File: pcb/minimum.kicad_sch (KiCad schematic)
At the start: 24 parts, among them J1 USB4155-03-C_REVA, U1 RP2040, U2 SCD4x, Y1 C2E-12.000-18-1020-X-R

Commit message: flash added
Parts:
- added U3: W25Q128JVPIM, SMD:W25Q128JVPIM, symbol W25Q128:W25Q128JVPIM
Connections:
- net +3V3: now also U3.8 (VCC)
- net GND: now also U3.4 (GND)
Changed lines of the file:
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@@
+    (pin "1")
+  )
+  (symbol (lib_id "power:+3V3") (at 55.245 147.32 0) (unit 1)
+    (in_bom yes) (on_board yes) (fields_autoplaced)
+    (property "Reference" "#PWR0117" (id 0) (at 55.245 151.13 0)
+      (effects (font (size 1.27 1.27)) hide)
+    )
+    (property "Value" "+3V3" (id 1) (at 55.245 143.7154 0))
+    (property "Footprint" "" (id 2) (at 55.245 147.32 0)
+      (effects (font (size 1.27 1.27)) hide)
+    )
+    (property "Datasheet" "" (id 3) (at 55.245 147.32 0)
+      (effects (font (size 1.27 1.27)) hide)
+    )
     (pin "1")
   )
@@
     )
     (property "Datasheet" "" (id 3) (at 53.975 108.585 0)
+      (effects (font (size 1.27 1.27)) hide)
+    )
+    (pin "1")
+  )
+  (symbol (lib_id "power:GND") (at 55.245 188.595 0) (unit 1)
+    (in_bom yes) (on_board yes) (fields_autoplaced)
+    (property "Reference" "#PWR0118" (id 0) (at 55.245 194.945 0)
+      (effects (font (size 1.27 1.27)) hide)
+    )
+    (property "Value" "GND" (id 1) (at 55.245 193.1576 0))
+    (property "Footprint" "" (id 2) (at 55.245 188.595 0)
+      (effects (font (size 1.27 1.27)) hide)
+    )
+    (property "Datasheet" "" (id 3) (at 55.245 188.595 0)
       (effects (font (size 1.27 1.27)) hide)
     )
@@
     (pin "S1")
     (pin "S2")
+  )
+  (symbol (lib_id "W25Q128:W25Q128JVPIM") (at 55.245 167.64 0) (unit 1)
+    (in_bom yes) (on_board yes)
+    (property "Reference" "U3" (id 0) (at 44.1325 153.33 0)
+      (effects (font (size 1.524 1.524)))
+    )
+    (property "Value" "W25Q128JVPIM" (id 1) (at 54.9275 168.039 0)
+      (effects (font (size 1.524 1.524)))
+    )
+    (property "Footprint" "SMD:W25Q128JVPIM" (id 2) (at 80.645 182.499 0)
+      (effects (font (size 1.524 1.524)) hide)
+    )
+    (property "Datasheet" "" (id 3) (at 37.465 188.595 0)
+      (effects (font (size 1.524 1.524)))
+    )
+    (pin "1")
+    (pin "2")
+    (pin "3")
+    (pin "4")
+    (pin "5")
+    (pin "6")
+    (pin "7")
+    (pin "8")
   )
   (symbol (lib_id "MCU_RaspberryPi_and_Boards:RP2040") (at 142.875 95.25 0) (unit 1)
@@
       (reference "#PWR0116") (unit 1) (value "GND") (footprint "")
     )
+    (path "/fc3e5b1f-88e5-4c63-9aca-ca6175ded61f"
+      (reference "#PWR0117") (unit 1) (value "+3V3") (footprint "")
+    )
+    (path "/6a7218c7-5bbe-4810-abcb-4070268ac5f6"
+      (reference "#PWR0118") (unit 1) (value "GND") (footprint "")
+    )
     (path "/e7effd1f-dcf0-44f9-acf3-2bc5919ae9df"
       (reference "C1") (unit 1) (value "100n") (footprint "Capacitor_SMD:C_0402_1005Metric")
@@
       (reference "U2") (unit 1) (value "SCD4x") (footprint "SMD:QFN-20_EP_10.1x10.1_Pitch1.25mm")
     )
+    (path "/62b39fed-7c45-4e1a-95a8-2a2f9be3c7c9"
+      (reference "U3") (unit 1) (value "W25Q128JVPIM") (footprint "SMD:W25Q128JVPIM")
+    )
     (path "/37671b67-047c-485d-9225-8788fbc7a0bf"

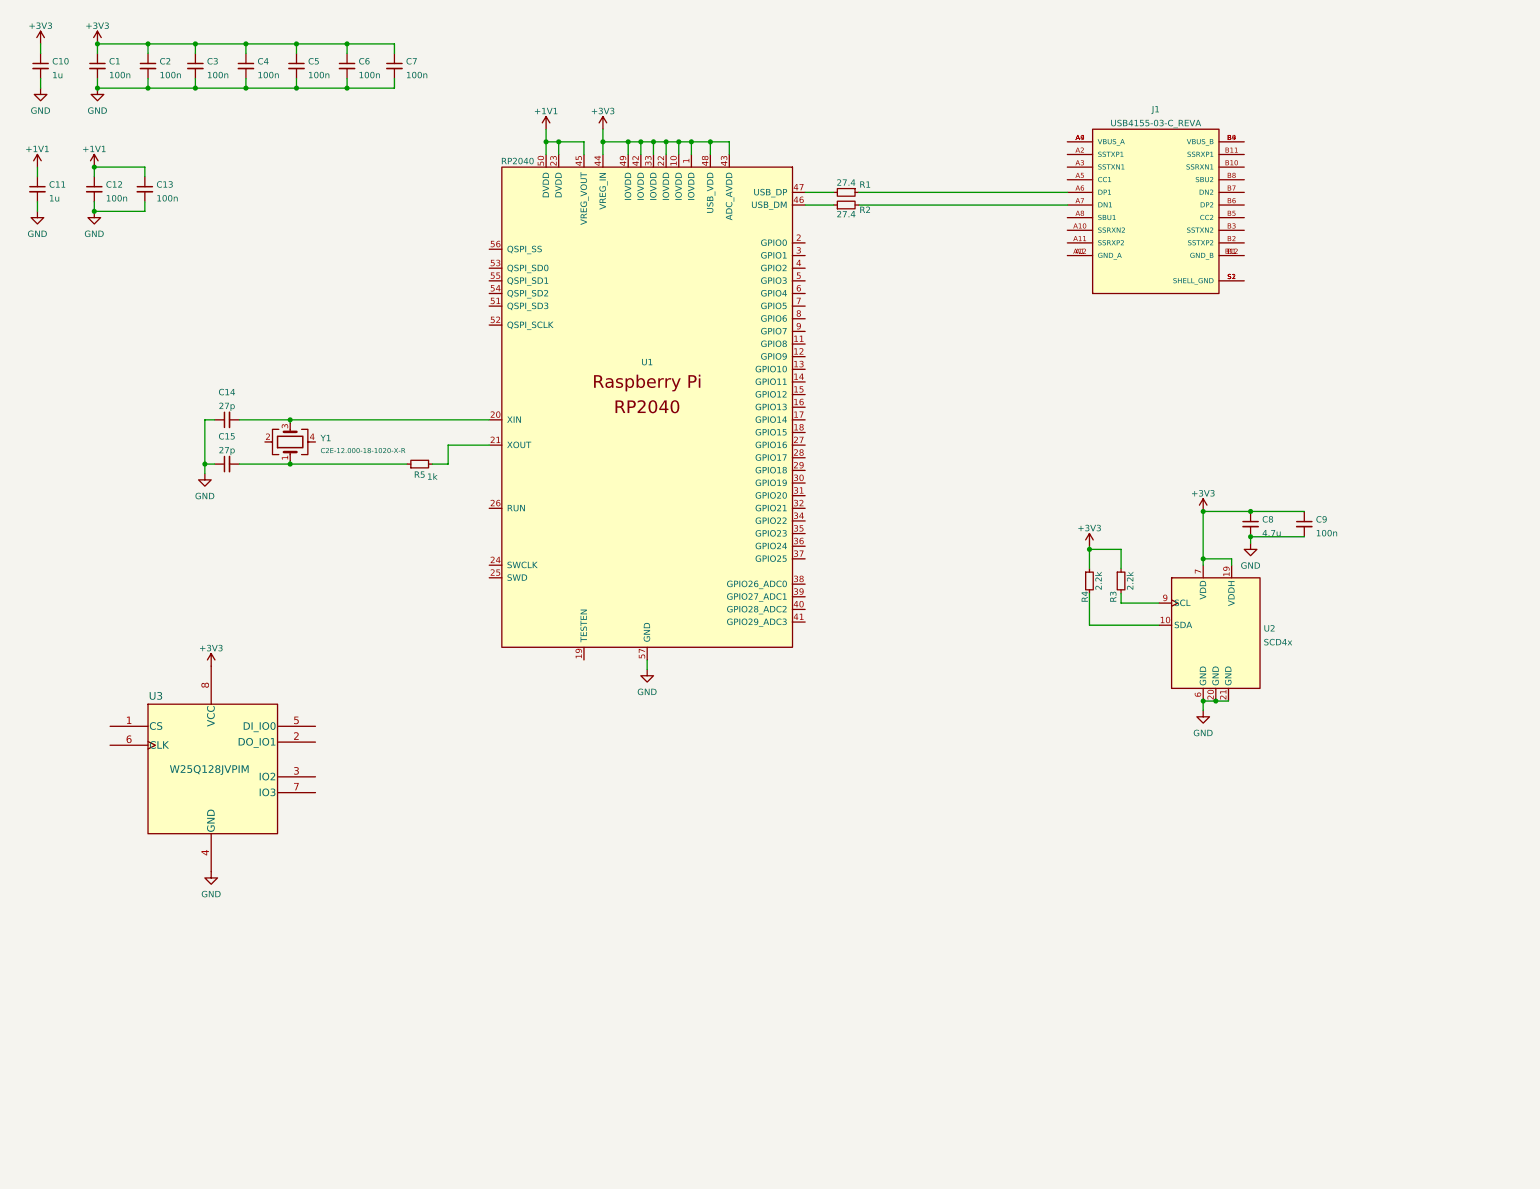
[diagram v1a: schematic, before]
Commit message: connecting signals
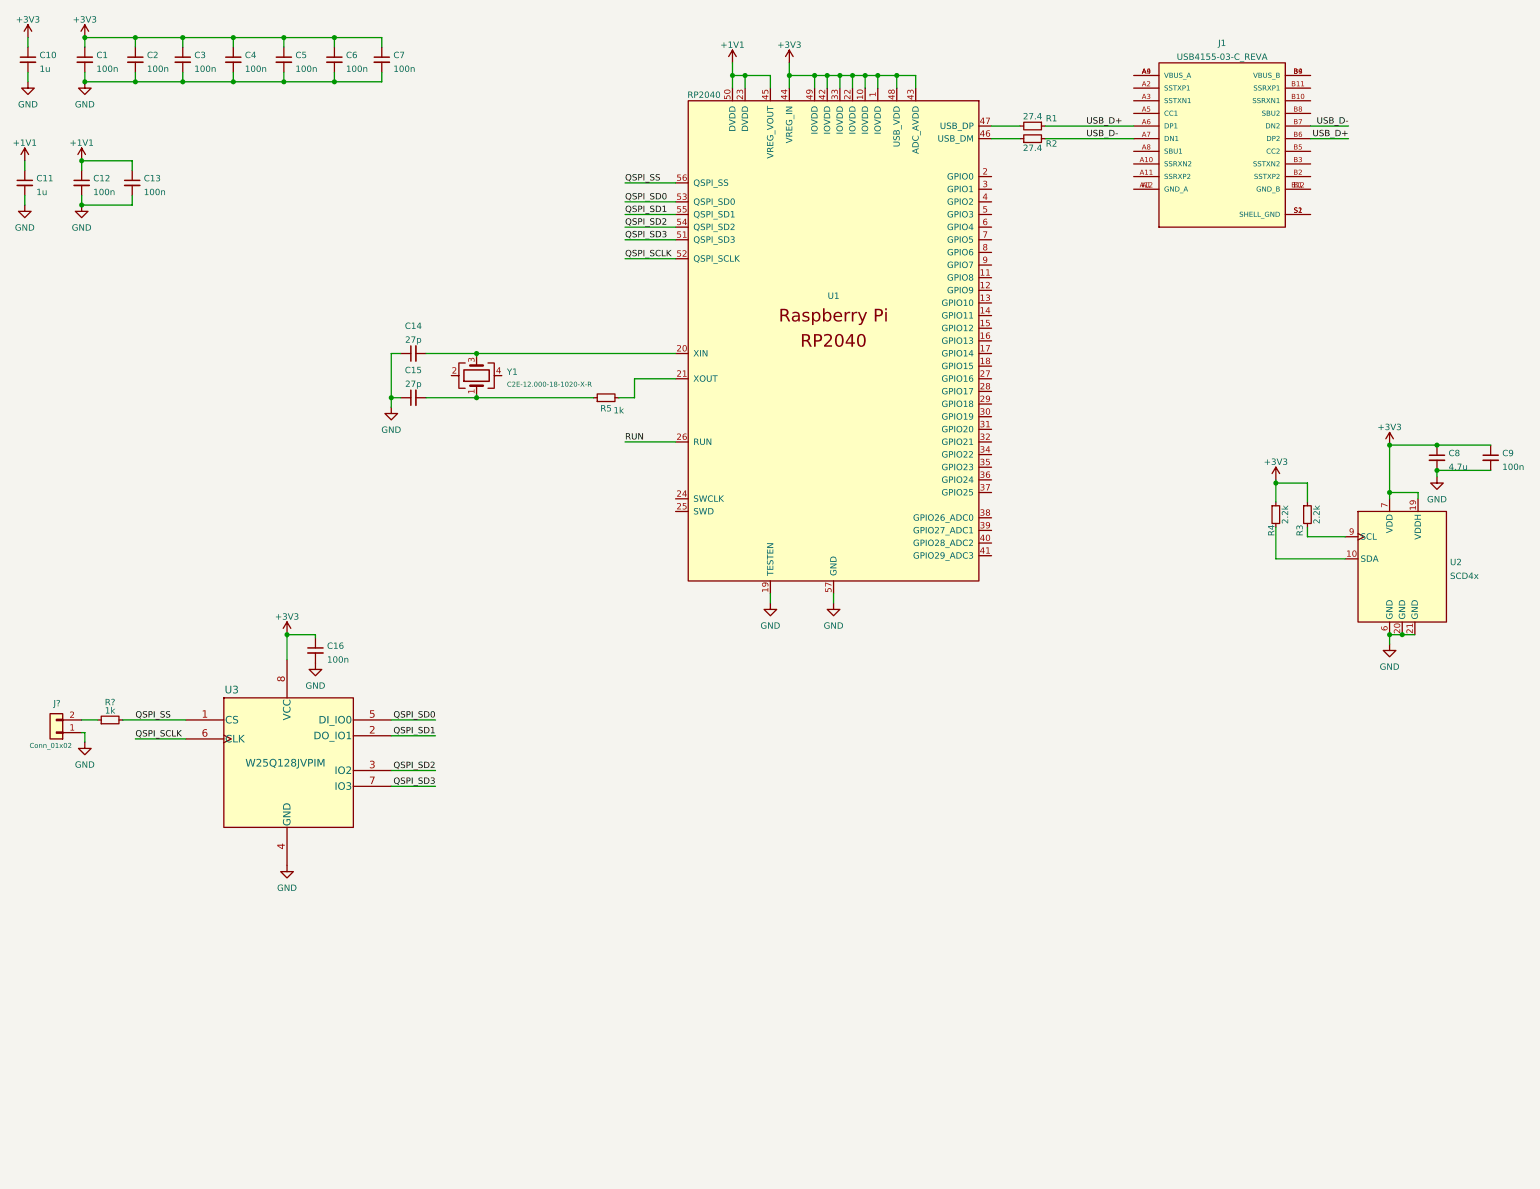
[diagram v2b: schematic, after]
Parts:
- added C16: 100n, Capacitor_SMD:C_0402_1005Metric, symbol Device:C_Small
- added J?: Conn_01x02, symbol Connector_Generic:Conn_01x02
- added R?: 1k, Resistor_SMD:R_0402_1005Metric, symbol Device:R_Small
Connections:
- net +3V3: now also C16.1
- net GND: now also U1.19 (TESTEN), C16.2, J?.1 (Pin_1)
- net QSPI_SS: now reaches U3.1 (CS)
- net QSPI_SS: now also U1.56 (QSPI_SS), R?.2
- net QSPI_SD1: now reaches U3.2 (DO_IO1)
- net QSPI_SD1: now also U1.55 (QSPI_SD1)
- net QSPI_SD2: now reaches U3.3 (IO2)
- net QSPI_SD2: now also U1.54 (QSPI_SD2)
- net QSPI_SD0: now reaches U3.5 (DI_IO0)
- net QSPI_SD0: now also U1.53 (QSPI_SD0)
- net QSPI_SCLK: now reaches U3.6 (CLK)
- net QSPI_SCLK: now also U1.52 (QSPI_SCLK)
- net QSPI_SD3: now reaches U3.7 (IO3)
- net QSPI_SD3: now also U1.51 (QSPI_SD3)
- net RUN: now reaches U1.26 (RUN)
- net USB_D+: now reaches J1.A6 (DP1), R1.1
- net USB_D+: now also J1.B6 (DP2)
- net USB_D-: now reaches J1.A7 (DN1), R2.2
- net USB_D-: now also J1.B7 (DN2)
- new net: J?.2 (Pin_2), R?.1
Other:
- moved on the sheet: C1, C10, C11, C12, C13, C14, C15, C2, C3, C4, C5, C6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

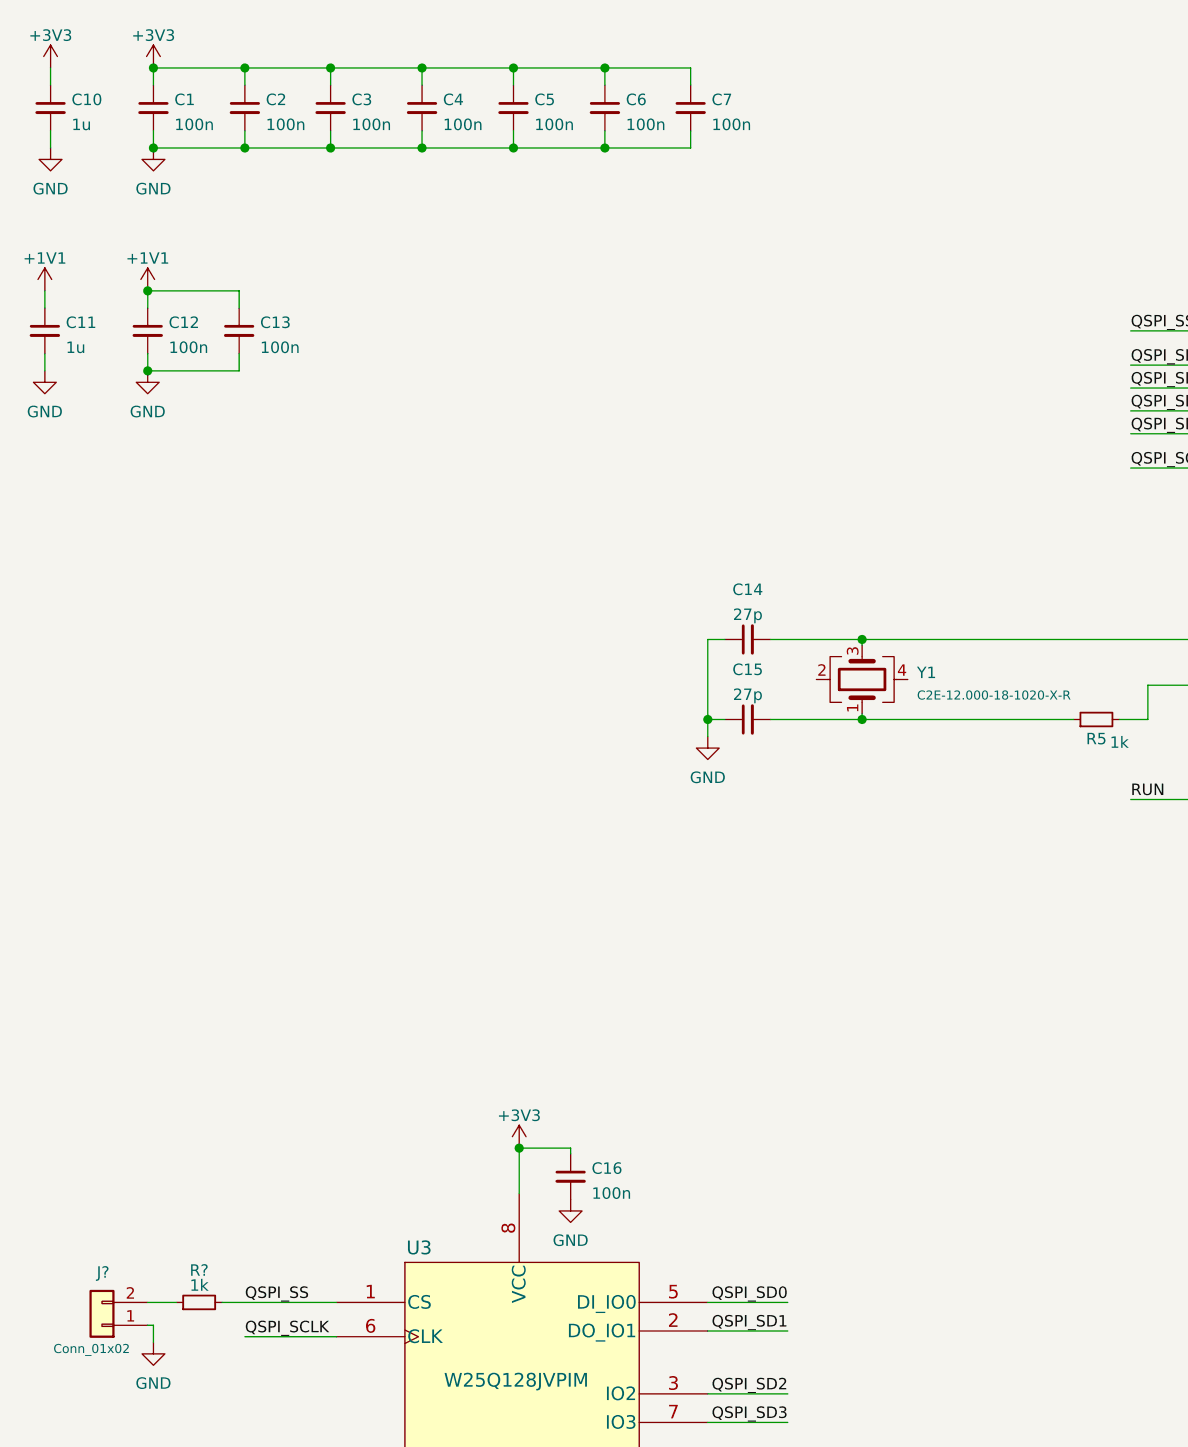
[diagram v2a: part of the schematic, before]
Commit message: connecting signals
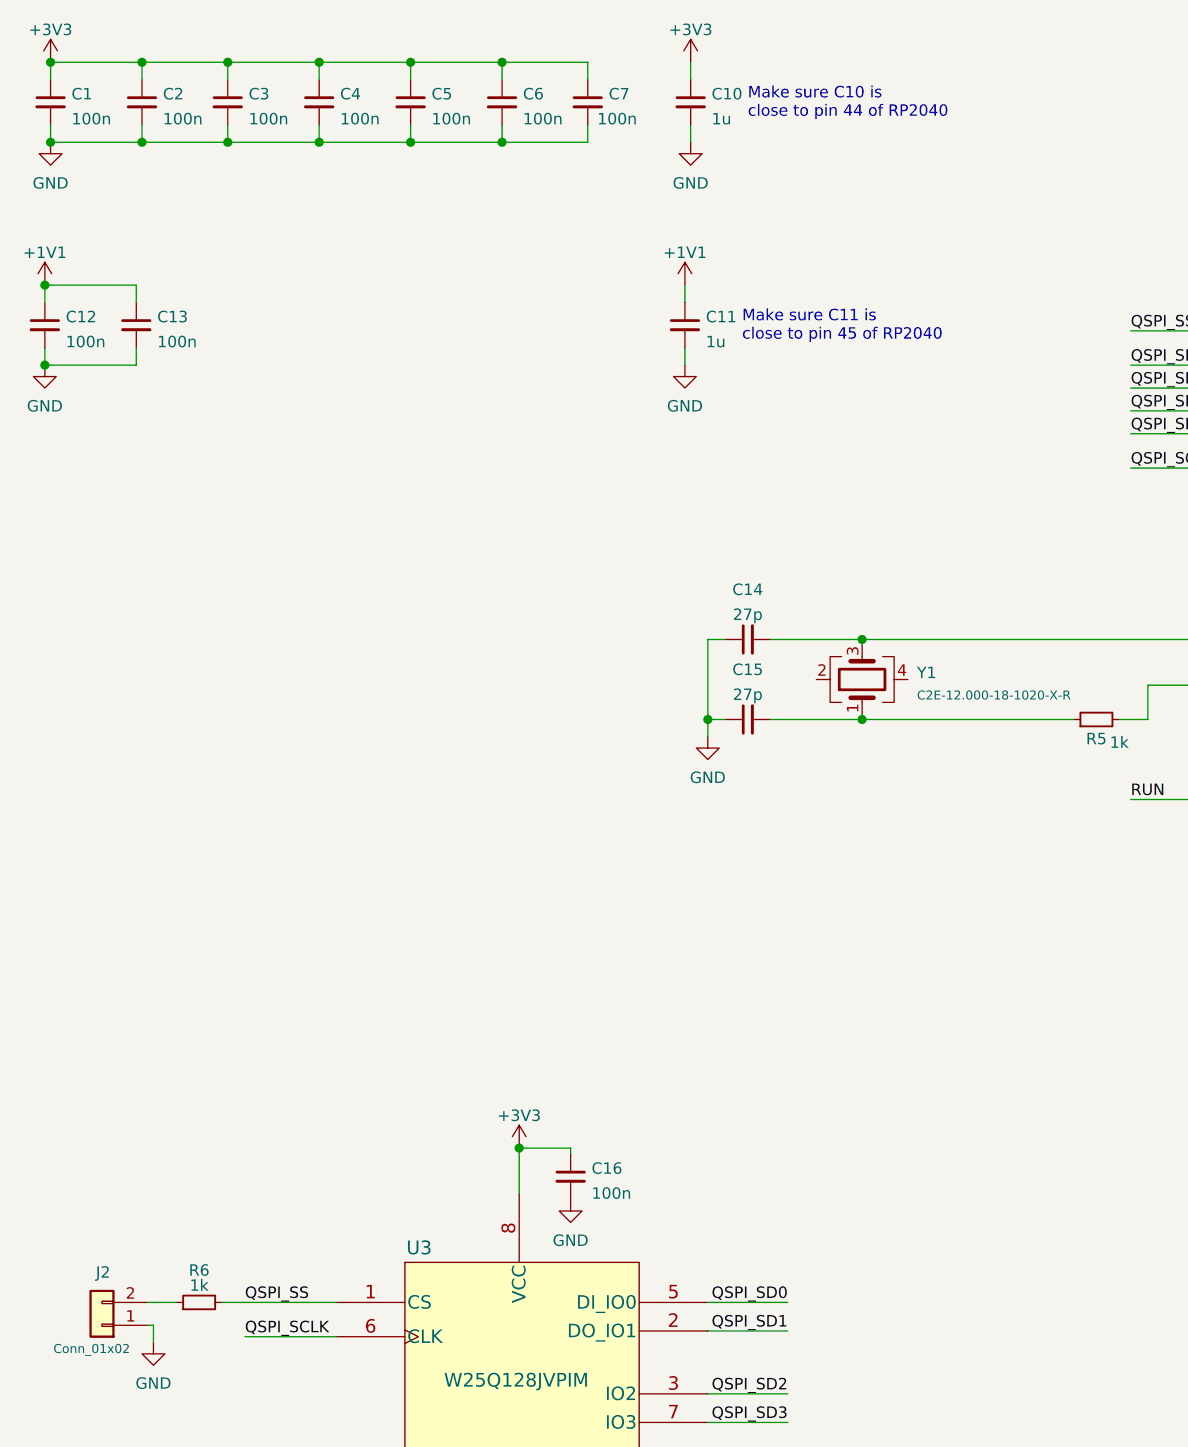
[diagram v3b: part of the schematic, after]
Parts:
- gave numbers to parts that had none: 2
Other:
- note added: "Make sure C10 is close to pin 44 of RP2040"
- note added: "Make sure C11 is close to pin 45 of RP2040"
- moved on the sheet: C1, C10, C11, C12, C13, C2, C3, C4, C5, C6, C7

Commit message: flash changed due to space constrains
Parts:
- U3: value W25Q128JVPIM -> W25Q16JVUXIQ; footprint SMD:W25Q128JVPIM -> SMD:W25Q16JVUXIQ
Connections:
- net XIN: now reaches C14.2, U1.20 (XIN), Y1.3
- net XOUTc: now reaches C15.2, R5.1, Y1.1
- net XOUT: now reaches R5.2, U1.21 (XOUT)
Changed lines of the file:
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@@
     (effects (font (size 1.27 1.27)) (justify right bottom))
+  )
+  (label "XIN" (at 108.585 84.455 0)
+    (effects (font (size 1 1)) (justify left bottom))
+  )
+  (label "XOUTc" (at 131.953 93.345 180)
+    (effects (font (size 1 1)) (justify right bottom))
   )
   (label "QSPI_SS" (at 138.43 50.165 0)
@@
   (label "RUN" (at 138.43 102.235 0)
     (effects (font (size 1.27 1.27)) (justify left bottom))
+  )
+  (label "XOUT" (at 140.335 93.345 0)
+    (effects (font (size 1 1)) (justify left bottom))
   )
   (label "USB_D+" (at 231.14 38.735 0)
@@
       (effects (font (size 1.524 1.524)))
     )
-    (property "Value" "W25Q128JVPIM" (id 1) (at 70.1675 166.769 0)
+    (property "Value" "W25Q16JVUXIQ" (id 1) (at 70.1675 166.769 0)
       (effects (font (size 1.524 1.524)))
     )
-    (property "Footprint" "SMD:W25Q128JVPIM" (id 2) (at 95.885 181.229 0)
+    (property "Footprint" "SMD:W25Q16JVUXIQ" (id 2) (at 95.885 181.229 0)
       (effects (font (size 1.524 1.524)) hide)
     )
@@
     )
     (path "/62b39fed-7c45-4e1a-95a8-2a2f9be3c7c9"
-      (reference "U3") (unit 1) (value "W25Q128JVPIM") (footprint "SMD:W25Q128JVPIM")
+      (reference "U3") (unit 1) (value "W25Q16JVUXIQ") (footprint "SMD:W25Q16JVUXIQ")
     )
     (path "/37671b67-047c-485d-9225-8788fbc7a0bf"

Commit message: routing
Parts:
- added C17, C18: 10u, Capacitor_SMD:C_0603_1608Metric, symbol Device:C_Small
- added R7: 10k, Resistor_SMD:R_0402_1005Metric, symbol Device:R_Small
- added U4: XCL220, SMD:XCL220, symbol torex:XCL220
- Y1: footprint (none) -> SMD:AKER_C2E
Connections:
- net +3V3: now also C18.1, U4.3 (Vout), U4.8 (L2)
- net GND: now also Y1.2, Y1.4, C18.2, U4.2 (AGND), U4.5 (PGND), U4.PAD
- net SCL: now reaches R3.2, U2.9 (SCL)
- net SDA: now reaches R4.2, U2.10 (SDA)
- net VBUS: now reaches J1.A4 (VBUS_A), J1.A9 (VBUS_A)
- net VBUS: now also J1.B4 (VBUS_B), J1.B9 (VBUS_B)
- new net: R7.2, U4.4 (CE)
- new net: U4.1 (Lx), U4.7 (L1)
- new net +5V: R7.1, U4.6 (Vin)
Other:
- moved on the sheet: C16, C8, C9, J2, R3, R4, R6, U2, U3

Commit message: routing
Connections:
- net SCL: now also U1.14 (GPIO11)
- net SDA: now also U1.13 (GPIO10)
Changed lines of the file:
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@@
+    (stroke (width 0) (type solid) (color 0 0 0 0))
+  )
+  (wire (pts (xy 212.09 74.295) (xy 220.345 74.295))
+    (stroke (width 0) (type solid) (color 0 0 0 0))
+  )
+  (wire (pts (xy 212.09 76.835) (xy 220.345 76.835))
     (stroke (width 0) (type solid) (color 0 0 0 0))
   )
@@
     (effects (font (size 1 1)) (justify left bottom))
   )
+  (label "SDA" (at 220.345 74.295 180)
+    (effects (font (size 1.27 1.27)) (justify right bottom))
+  )
+  (label "SCL" (at 220.345 76.835 180)
+    (effects (font (size 1.27 1.27)) (justify right bottom))
+  )
   (label "USB_D+" (at 231.14 38.735 0)
